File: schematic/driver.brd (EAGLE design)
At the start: 61.9 x 36.8 mm, 58 parts

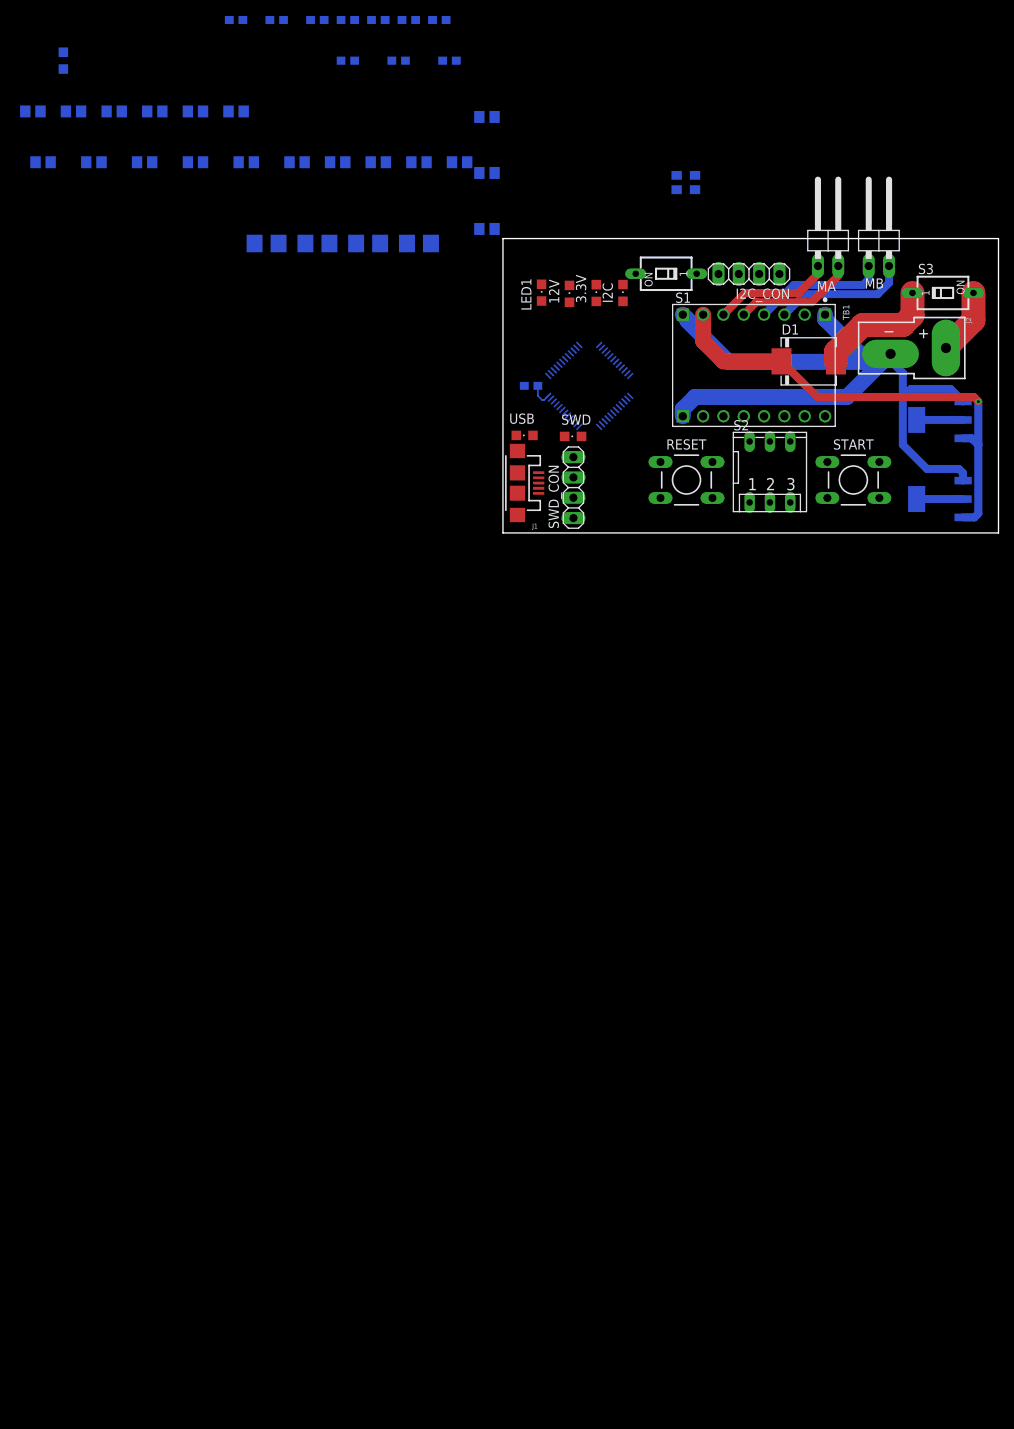
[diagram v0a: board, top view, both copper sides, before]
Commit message: Add in series stabilisators
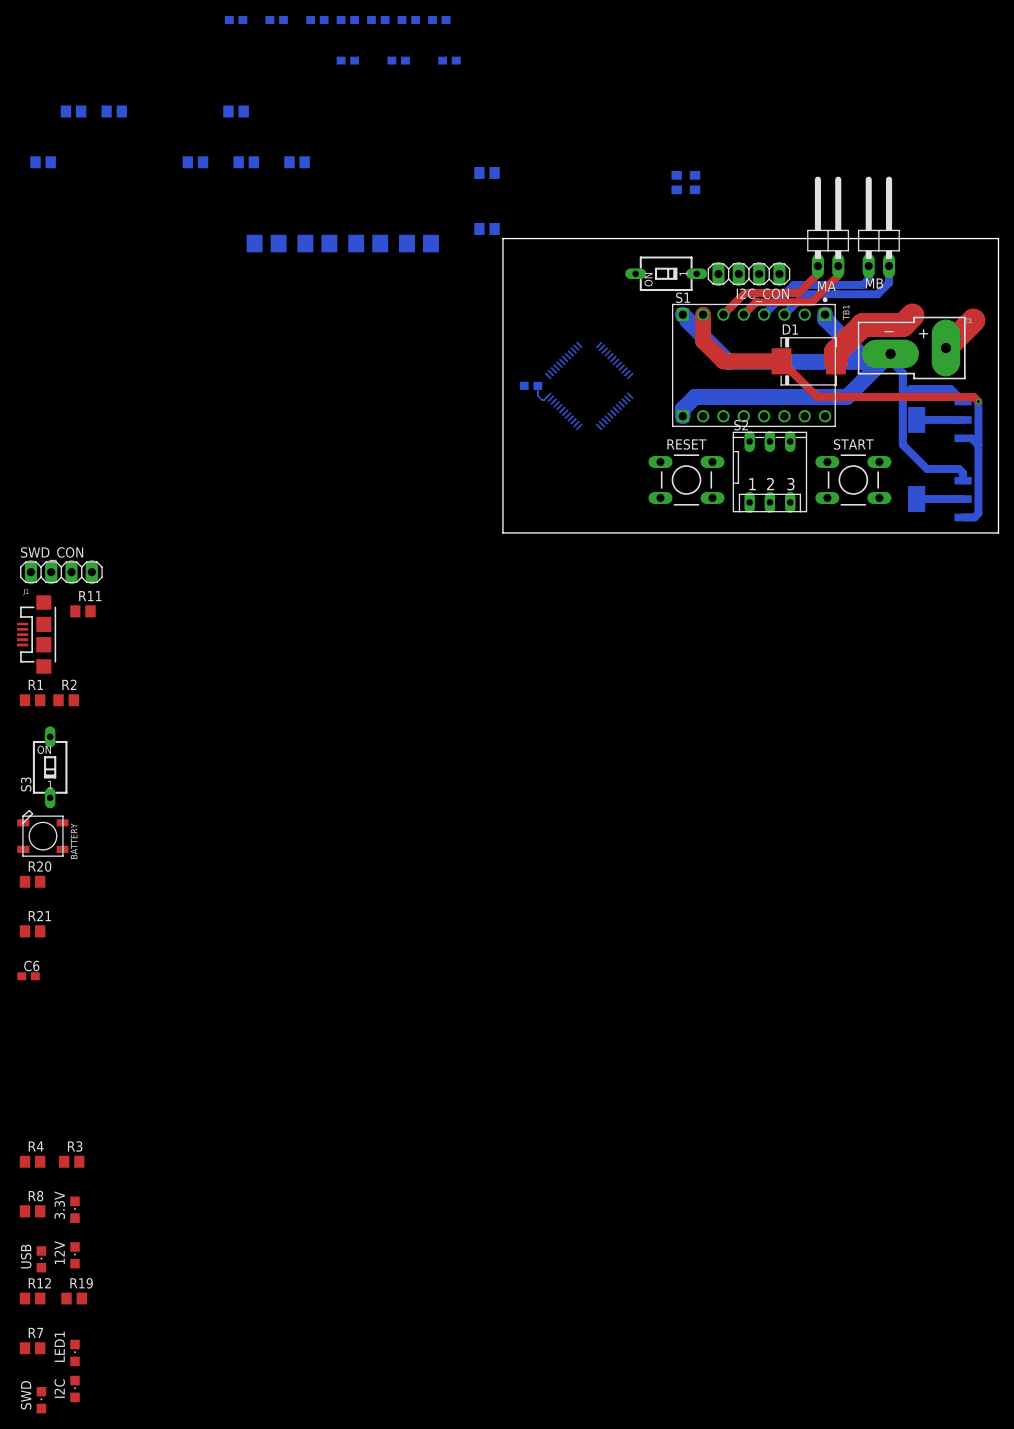
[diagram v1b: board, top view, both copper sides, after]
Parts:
- removed R13: 65, rcl:R0805
- added C6: 100n, rcl:C0603
- added R20: 150R, rcl:R0805
- added R21: 33R, rcl:R0805
- BATTERY: value (none) -> WS2812B5050; device led:CHIPLED_0805 -> adafruit:WS2812B
- moved R19 156.5 mm to (-53.6, -95.7), flipped to the top
- moved R7 155.3 mm to (-58.8, -101.9), flipped to the top
- moved I2C 153.2 mm to (-53.5, -107.0)
- moved LED1 144.8 mm to (-53.5, -102.5)
- moved R12 142.2 mm to (-58.8, -95.7), flipped to the top
- moved R8 139.0 mm to (-58.8, -84.8), flipped to the top
- moved SWD 137.6 mm to (-57.7, -108.4), turned to 0 degrees
- moved 12V 135.2 mm to (-53.5, -90.3)
- moved R4 132.2 mm to (-58.8, -78.6), flipped to the top
- moved 3.3V 131.8 mm to (-53.5, -84.6)
- moved R3 131.4 mm to (-53.9, -78.6), flipped to the top
- moved S3 126.4 mm to (-56.6, -29.3), turned to 0 degrees
- moved USB 119.4 mm to (-57.7, -90.8), turned to 0 degrees
- moved BATTERY 97.0 mm to (-57.5, -37.9), flipped to the top
- moved R2 83.3 mm to (-54.6, -20.9), flipped to the top
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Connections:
- removed net N$8: BATTERY.A, R13.1
- new net DI_LED: R21.2
- new net N$15: BATTERY.1-VDD, R20.1
- new net N$16: BATTERY.4-DIN, R21.1
- net GND: now also BATTERY.3-GND, C6.2; no longer BATTERY.C
- net LED2: no longer R13.2
- net STAB: no longer C13.+, LM1117.3
- net VCC: now also C13.+, J1.VBUS, LM1117.3, R11.2
- net VDD: now also C6.1, R20.2; no longer J1.VBUS, R11.2
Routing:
- net BAT+: track 8.30 -> 4.86 mm
- net DIODE: track 15.4 -> 12.6 mm
- net STAB: track 59.2 -> 58.1 mm

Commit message: update
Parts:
- removed S1: (no value), switch-dil:SD4-01
- added STM1: STM32F10XCXT6, stm32:TQFP48
- added U1: GY-521MPU6050, gy-521:GY-521
- S2: device switch-dil:DP-03 -> special:EDG-04
- moved D1 174.7 mm to (-56.1, -125.6)
- moved R8 49.1 mm to (-58.8, -133.9)
- moved USB 49.1 mm to (-57.7, -139.9)
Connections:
- removed net TDO: STM32.39
- new net INT: STM32.39, U1.INT
- new net VBAT: STM1.1
- new net VDDA: STM1.9
- new net VDD_1: STM1.24
- new net VDD_2: STM1.36
- new net VDD_3: STM1.48
- new net VSSA: STM1.8
- new net VSS_1: STM1.23
- new net VSS_2: STM1.35
- new net VSS_3: STM1.47
- net GND: now also STM1.44, U1.GND; no longer STM32.44
- net NRST: now also STM1.7; no longer STM32.7
- net PC13: no longer R7.2
- net SCL: now also U1.SCL
- net SDA: now also U1.SDA
- net SWDIO: now also R7.2
- net VCC: now also S2.5, U1.VCC; no longer S1.2
- net VCC_S: now also S2.4; no longer S1.1
- net VDD: now also S2.7, S2.8; no longer S2.4, S2.5
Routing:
- net STAB: track 58.1 -> 44.6 mm
- net DIODE: track 12.6 -> 0.00 mm

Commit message: added charger, and over charge protection
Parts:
- removed BATTERY: WS2812B5050, adafruit:WS2812B
- removed I2C: (no value), led:CHIPLED_0805
- added C12, C20, C21, C7, C8: 100n, rcl:C0603
- added D2, D3, D4, D5, D6, D7: S3A, s3x_10:DO214AB
- added IC1, IC2, IC3: DW01A, DW01A:SOT23-6
- added LCD1: LPH-7366, lph-7366 (1):LPH-7366
- added R13, R22, R24, R25, R27, R28, R29: 1k, rcl:R0805
- added R23, R26: 10k, rcl:R0805
- added R30, R31, R32: 100, rcl:R0805
- added U$1, U$2, U$3: TP4056, TP4056:SOT23-8
- R19: value 65 -> 1k
- R20: value 150R -> 10k
- R21: value 33R -> 1k
- moved R21 171.9 mm to (-94.4, -218.0)
- moved R20 163.3 mm to (-101.0, -201.4)
- moved C6 142.3 mm to (-82.4, -195.8)
- moved R19 98.6 mm to (-81.9, -190.2)
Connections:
- removed net DI_LED: R21.2
- new net CELL1: R30.2, U$1.5
- new net CELL2: R31.2, U$2.5
- new net CELL3: R32.2, U$3.5
- new net D/C: LCD1.4
- new net MOSI: LCD1.3
- new net N$12: D2.C, R13.1
- new net N$13: R19.2, U$1.7
- new net N$14: D3.C, R19.1
- new net N$18: D4.C, R21.1
- new net N$19: D5.C, R22.1
- new net N$20: R23.2, U$2.2
- new net N$21: LCD1.8
- new net N$22: R25.2, U$3.7
- new net N$23: R24.2, U$3.6
- new net N$24: D6.C, R24.1
- new net N$25: D7.C, R25.1
- new net N$26: R26.2, U$3.2
- new net N$27: C20.1, C21.1, IC2.5, IC3.5, R30.1, R31.1
- new net N$28: IC3.2, R29.2
- new net N$29: C12.1, IC1.5, R32.1
- new net N$30: IC1.2, R27.2
- new net N$32: IC2.2, R28.2
- new net N$8: R22.2, U$2.7
- new net RES: LCD1.9
- new net SCE: LCD1.5
- new net SCLK: LCD1.2
- net GND: now also C12.2, C20.2, C21.2, C7.2, C8.2, IC1.6, IC2.6, IC3.6, LCD1.7, R20.1, R23.1, R26.1, R27.1, R28.1, R29.1, U$1.1, U$1.3, U$2.1, U$2.3, U$3.1, U$3.3; no longer BATTERY.3-GND, I2C.C
- net N$15: now also R20.2, U$1.2; no longer BATTERY.1-VDD, R20.1
- net N$16: now also R21.2, U$2.6; no longer BATTERY.4-DIN, R21.1
- net N$9: now also R13.2, U$1.6; no longer I2C.A, R19.1
- net VCC: now also C6.1, C7.1, C8.1, D2.A, D3.A, D4.A, D5.A, D6.A, D7.A, LCD1.6, U$1.4, U$1.8, U$2.4, U$2.8, U$3.4, U$3.8
- net VCC_S: no longer R19.2
- net VDD: now also LCD1.1; no longer C6.1, R20.2

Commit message: Added battery managment and motor drivers
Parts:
- removed J2: (no value), SparkFun-Connectors:DEANS
- removed LM1, LM1117: LM1117MP-3.3, lm1117_11:SOT223
- removed S3: (no value), switch-dil:SD4-01
- removed TB1: POLOLU-713, POLOLU-713:SHIELD_POLOLU-713
- added 7.5K: 7.5k, rcl:R0805
- added 7.5K1: 4.5k, rcl:R0805
- added D8: CESD5V0D1, Diodes:SOD-123
- added JP1: (no value), pinhead:1X03
- added JP2: (no value), pinhead:1X02
- added L1, L2: 22uH, rcl:L1812
- added Q2, Q3, Q4: SI1922EDH-T1-GE3, fets:SOT363
- added R33, R34: 1k, rcl:R0805
- added S4: (no value), switch:255SB
- added U$4, U$5: MT3608SOT23-6, MT3608:SOT23-6
- added U$6, U$7: TB6612FNG, TB6612FNG:SSOP24
- C13, C14, C18, C19: value 10u -> 100n; device rcl:CT3528 -> rcl:C0603
- D1: value S3A -> CESD5V0D1; device s3x_10:DO214AB -> Diodes:SOD-123
- moved C19 492.7 mm to (-104.4, -447.5), flipped to the top
- moved C18 492.5 mm to (-109.8, -447.5), flipped to the top
- moved C14 460.5 mm to (-115.0, -415.1), flipped to the top
- moved C13 454.5 mm to (-115.0, -410.2), flipped to the top
- moved D1 284.8 mm to (-113.4, -404.6)
- moved IC3 85.0 mm to (-100.6, -359.6)
- moved C21 82.2 mm to (-101.9, -373.1)
- moved IC2 71.8 mm to (-100.6, -338.7)
- moved C20 66.2 mm to (-101.9, -352.2)
- moved R29 65.0 mm to (-106.6, -373.7)
- moved R28 50.4 mm to (-106.6, -352.8)
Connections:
- removed net DIODE: D1.A, S3.1
- removed net N$42: MA.2, TB1.5
- removed net N$43: MA.1, TB1.6
- removed net N$44: MB.1, TB1.4
- removed net N$45: MB.2, TB1.3
- new net A01: MA.2, U$6.1, U$6.11, U$6.12, U$6.2
- new net A02: MB.2, U$7.1, U$7.11, U$7.12, U$7.2
- new net AO1: MB.1, U$7.5, U$7.6, U$7.7, U$7.8
- new net AO2: MA.1, U$6.5, U$6.6, U$6.7, U$6.8
- new net BAT_ON: C13.1, C18.1, L1.1, L2.1, S4.1, U$4.P$4, U$4.P$5, U$5.P$4, U$5.P$5, U$6.13, U$6.14, U$6.24, U$7.13, U$7.14, U$7.24
- new net N$28: IC1.3, Q2.5
- new net N$31: Q2.3, Q2.6
- new net N$33: C20.1, IC2.5, R31.1
- new net N$34: IC2.1, Q3.2
- new net N$35: IC2.3, Q3.5
- new net N$36: Q3.3, Q3.6
- new net N$38: C21.1, IC3.5, R30.1
- new net N$39: IC3.1, Q4.2
- new net N$40: IC3.3, Q4.5
- new net N$41: Q4.3, Q4.6
- new net N$47: D1.A, L1.2, U$4.P$1
- new net N$49: D8.A, L2.2, U$5.P$1
- new net N$50: 7.5K1.1, R33.2, U$5.P$3
- new net N$51: 7.5K.1, R34.2, U$4.P$3
- new net VBUS: J1.VBUS, JP1.2
- new net VUSB: C6.1, C7.1, C8.1, D2.A, D3.A, D4.A, D5.A, D6.A, D7.A, JP1.3, U$1.4, U$1.8, U$2.4, U$2.8, U$3.4, U$3.8
- net BAT+: now also JP2.2, R17.2, S4.2; no longer J2.+, S3.2
- net GND: now also C13.2, C14.2, C18.2, C19.2, JP2.1, Q2.1, Q2.4, Q3.1, Q3.4, Q4.1, Q4.4, R33.1, R34.1, U$4.P$2, U$5.P$2, U$6.10, U$6.18, U$6.3, U$6.4, U$6.9, U$7.10, U$7.18, U$7.3, U$7.4, U$7.9; no longer C13.-, C14.-, C18.-, C19.-, J2.-, LM1.1, LM1117.1, TB1.1, TB1.8, TB1.9
- net MA1: now also U$6.17, U$6.21; no longer TB1.14
- net MA2: now also U$6.16, U$6.22; no longer TB1.15
- net MB1: now also U$7.17, U$7.21; no longer TB1.12
- net MB2: now also U$7.16, U$7.22; no longer TB1.11
- net N$27: now also IC1.1, Q2.2; no longer C20.1, C21.1, IC2.5, IC3.5, R30.1, R31.1
- net PWMA: now also U$6.15, U$6.23; no longer TB1.16
- net PWMB: now also U$7.15, U$7.23; no longer TB1.10
- net STAB: no longer C18.+, D1.C, LM1.3, R17.2, TB1.7
- net VCC: now also 7.5K.2, C14.1, D1.C, JP1.1, U$6.19, U$6.20, U$7.19, U$7.20; no longer C13.+, C19.+, C6.1, C7.1, C8.1, D2.A, D3.A, D4.A, D5.A, D6.A, D7.A, J1.VBUS, LM1.2, LM1.4, LM1117.3, TB1.13, TB1.2, U$1.4, U$1.8, U$2.4, U$2.8, U$3.4, U$3.8
- net VDD: now also 7.5K1.2, C19.1, D8.C; no longer C14.+, LM1117.2, LM1117.4
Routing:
- net GND: track 98.3 -> 0.00 mm
- net STAB: track 44.6 -> 0.00 mm, vias 1 -> 0
- net N$45: track 16.8 -> 0.00 mm
- net N$44: track 16.6 -> 0.00 mm
- net N$42: track 15.0 -> 0.00 mm
- net N$43: track 14.9 -> 0.00 mm
- net A02: track 0.00 -> 13.2 mm
- net A01: track 0.00 -> 12.8 mm
- net AO1: track 0.00 -> 11.3 mm
- net AO2: track 0.00 -> 11.1 mm
- net VDD: track 8.79 -> 2.99 mm
- net VCC: track 5.80 -> 0.00 mm
- net BAT+: track 4.86 -> 0.00 mm

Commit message: added MPU6050 to board, and two motor drivers
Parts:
- removed U1: GY-521MPU6050, gy-521:GY-521
- added C22, C23, C25, C27, C29, C31, C32: 100n, rcl:C0603
- added C24: 2.2n, rcl:C0603
- added C26: 10nF, rcl:C0603
- added C28, C30: 10uF, rcl:C0603
- added IC4: MPU6050, invensense:QFN50P400X400X95-25T265X275N
- moved U$5 7.16 mm to (-118.4, -435.2), turned to 90 degrees
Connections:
- new net N$42: C22.1, IC4.10
- new net N$43: C23.1
- new net N$44: IC4.11
- new net N$45: C24.1, IC4.20
- new net N$48: C27.1, C28.1, U$6.24
- net BAT_ON: now also C29.1, C30.1; no longer U$6.24
- net GND: now also C22.2, C23.2, C24.2, C25.2, C26.2, C27.2, C28.2, C29.2, C30.2, C31.2, C32.2, IC4.1, IC4.18, IC4.25; no longer U1.GND
- net INT: now also IC4.12; no longer U1.INT
- net SCL: now also IC4.23; no longer U1.SCL
- net SDA: now also IC4.24; no longer U1.SDA
- net VCC: now also C31.1, C32.1; no longer U1.VCC
- net VDD: now also C25.1, C26.1, IC4.13, IC4.8
